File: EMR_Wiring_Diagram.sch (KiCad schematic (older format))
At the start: 10 parts, among them SW1 Emergency Switch, SW2 Ignition Key

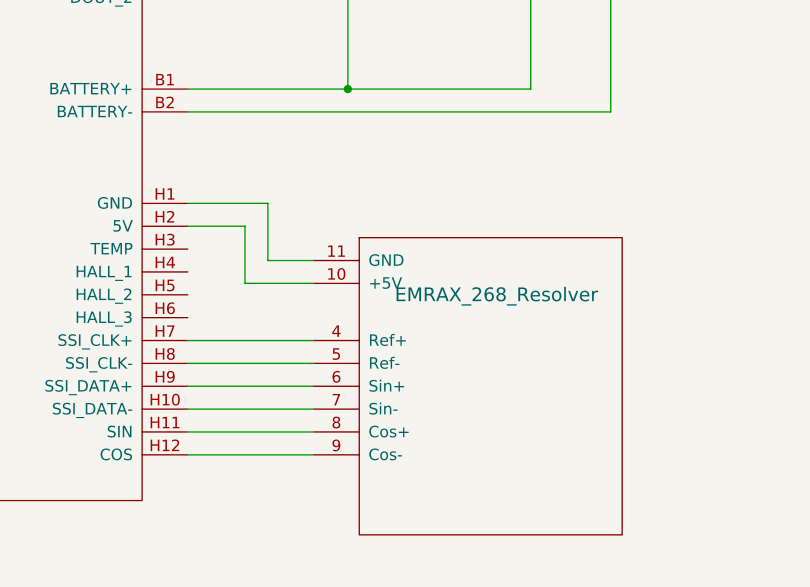
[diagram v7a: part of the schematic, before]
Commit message: Switched to SSI feedback
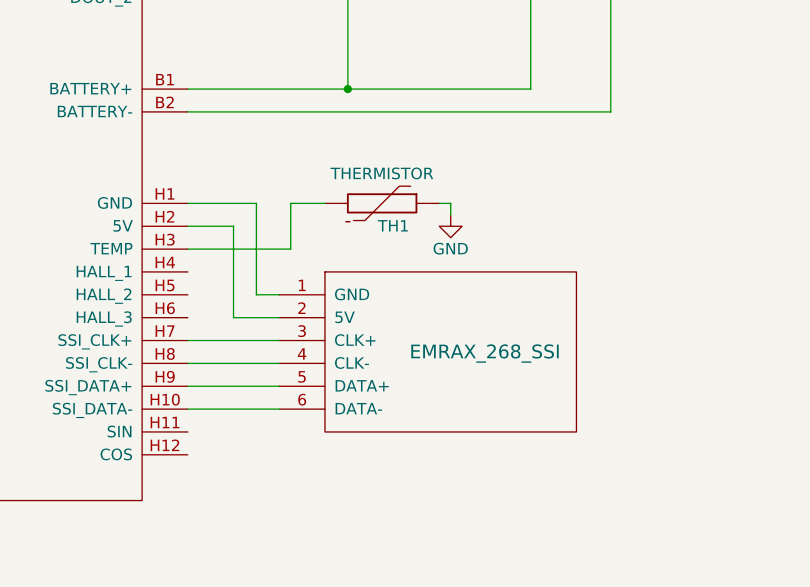
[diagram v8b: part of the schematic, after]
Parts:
- removed U?: EMRAX_268_Resolver, symbol EMRAX_268_Resolver
- added TH1: THERMISTOR, symbol THERMISTOR
- added U?: EMRAX_268_SSI, symbol EMRAX_268_SSI
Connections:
- net at U?.H1 (GND): now also U?.1 (GND)
- net at U?.H10 (SSI_DATA-): now also U?.6 (DATA-)
- net at U?.H2 (5V): now also U?.2 (5V)
- net at U?.H3 (TEMP): now also TH1.2
- net at U?.H7 (SSI_CLK+): now also U?.3 (CLK+)
- net at U?.H8 (SSI_CLK-): now also U?.4 (CLK-)
- net at U?.H9 (SSI_DATA+): now also U?.5 (DATA+)
- new net GND: TH1.1
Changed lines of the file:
@@
-$EndComp
-$Comp
-L EMRAX_268_Resolver U?
-U 1 1 56B01C7F
-P 8500 4400
-F 0 "U?" H 8500 4400 60  0001 C CNN
-F 1 "EMRAX_268_Resolver" H 8500 4400 60  0000 C CNN
-F 2 "" H 8500 4400 60  0000 C CNN
-F 3 "" H 8500 4400 60  0000 C CNN
-	1    8500 4400
-	1    0    0    -1
 $EndComp
 $Comp
@@
 	4000 4100 4150 4100
 Wire Wire Line
-	7700 4600 7150 4600
-Wire Wire Line
-	7700 4700 7150 4700
-Wire Wire Line
-	7700 4800 7150 4800
-Wire Wire Line
-	7700 4900 7150 4900
-Wire Wire Line
-	7700 5000 7150 5000
-Wire Wire Line
-	7700 5100 7150 5100
-Wire Wire Line
-	7700 4250 7500 4250
-Wire Wire Line
-	7700 4350 7400 4350
-Wire Wire Line
-	7400 4350 7400 4100
-Wire Wire Line
-	7400 4100 7150 4100
-Wire Wire Line
 	8600 1150 8500 1150
 Wire Wire Line
@@
 Wire Wire Line
 	8650 3500 8650 2850
-Wire Wire Line
-	7150 4000 7500 4000
-Wire Wire Line
-	7500 4000 7500 4250
 $Comp
 L Earth #PWR?
@@
 	1    0    0    -1
 $EndComp
+$Comp
+L EMRAX_268_SSI U?
+U 1 1 56B4CDC4
+P 8300 4650
+F 0 "U?" H 8300 4650 60  0001 C CNN
+F 1 "EMRAX_268_SSI" H 8450 4650 60  0000 C CNN
+F 2 "" H 8300 4650 60  0000 C CNN
+F 3 "" H 8300 4650 60  0000 C CNN
+	1    8300 4650
+	1    0    0    -1
+$EndComp
+Wire Wire Line
+	7550 4900 7150 4900
+Wire Wire Line
+	7550 4800 7150 4800
+Wire Wire Line
+	7150 4700 7550 4700
+Wire Wire Line
+	7550 4600 7150 4600
+Wire Wire Line
+	7550 4500 7350 4500
+Wire Wire Line
+	7350 4500 7350 4100
+Wire Wire Line
+	7350 4100 7150 4100
+Wire Wire Line
+	7450 4400 7550 4400
+Wire Wire Line
+	7450 4000 7150 4000
+Wire Wire Line
+	7450 4000 7450 4400
+$Comp
+L THERMISTOR TH1
+U 1 1 56B4D7ED
+P 8000 4000
+F 0 "TH1" V 8100 4050 50  0000 C CNN
+F 1 "THERMISTOR" V 7900 4000 50  0000 C BNN
+F 2 "" H 8000 4000 50  0000 C CNN
+F 3 "" H 8000 4000 50  0000 C CNN
+	1    8000 4000
+	0    1    1    0
+$EndComp
+$Comp
+L GND #PWR?
+U 1 1 56B4D836
+P 8300 4050
+F 0 "#PWR?" H 8300 3800 50  0001 C CNN
+F 1 "GND" H 8300 3900 50  0000 C CNN
+F 2 "" H 8300 4050 50  0000 C CNN
+F 3 "" H 8300 4050 50  0000 C CNN
+	1    8300 4050
+	1    0    0    -1
+$EndComp
+Wire Wire Line
+	8250 4000 8300 4000
+Wire Wire Line
+	8300 4000 8300 4050
+Wire Wire Line
+	7750 4000 7600 4000
+Wire Wire Line
+	7600 4000 7600 4200
+Wire Wire Line
+	7600 4200 7150 4200
 $EndSCHEMATC
